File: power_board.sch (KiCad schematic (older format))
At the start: 13 parts, among them J1 CONN_01X05, P1 BATT, Q1 DMP1045U, U1 MCP73831T-2ACI_OT

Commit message: Update for LIPO power_board
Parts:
- removed Q1: DMP1045U, TO_SOT_Packages_SMD:SOT-23, symbol Device:Q_PMOS_DGS
- added H1: MH2.1mm, my-fp-library:MH2.1mm, symbol marks:MH2.1mm
- added Q1: Q_PMOS_GSD (DMP1045U), TO_SOT_Packages_SMD:SOT-23, symbol Device:Q_PMOS_GSD
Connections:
- net labels added: D, G, S, VDD
- net labels removed: VSS
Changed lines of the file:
@@
 	6500 3650 6500 3800
 Connection ~ 6150 3400
-$Comp
-L Device:Q_PMOS_DGS Q1
-U 1 1 5C2824E1
-P 7100 3500
-AR Path="/5C2824E1" Ref="Q1"  Part="1"
-AR Path="/5C2799D2/5C2824E1" Ref="Q1"  Part="1"
-F 0 "Q1" H 7300 3550 50  0000 L CNN
-F 1 "DMP1045U" H 7300 3450 50  0000 L CNN
-F 2 "TO_SOT_Packages_SMD:SOT-23" H 7300 3600 50  0001 C CNN
-F 3 "" H 7100 3500 50  0000 C CNN
-	1    7100 3500
-	0    -1   -1   0
-$EndComp
 Wire Wire Line
 	3750 3400 3750 4050
@@
 F 6 "Microchip MCP73831T-2ACI/OT" H 5150 2600 50  0001 C CNN "BOM"
 	1    5150 3200
-	1    0    0    -1
+	1    0    0    1
 $EndComp
 Connection ~ 5850 3350
@@
 	4150 3000 4150 3250
 Text GLabel 3150 3400 0    50   Input ~ 0
-VSS
+VDD
 Text GLabel 2250 3650 2    50   Input ~ 0
-VSS
+VDD
 Text GLabel 8000 3050 2    50   Output ~ 0
 +5V
@@
 Wire Wire Line
 	2400 4050 2400 4200
+$Comp
+L marks:MH2.1mm H1
+U 1 1 5C3B8630
+P 8300 4500
+F 0 "H1" H 8400 4500 60  0001 C CNN
+F 1 "MH2.1mm" H 8300 4800 60  0001 C CNN
+F 2 "my-fp-library:MH2.1mm" H 8300 4500 60  0001 C CNN
+F 3 "" H 8300 4500 60  0001 C CNN
+	1    8300 4500
+	1    0    0    -1
+$EndComp
+$Comp
+L Device:Q_PMOS_GSD Q1
+U 1 1 5C4DD92F
+P 7100 3500
+F 0 "Q1" V 7443 3500 50  0000 C CNN
+F 1 "Q_PMOS_GSD (DMP1045U)" V 7352 3500 50  0000 C CNN
+F 2 "TO_SOT_Packages_SMD:SOT-23" H 7300 3600 50  0001 C CNN
+F 3 "~" H 7100 3500 50  0001 C CNN
+	1    7100 3500
+	0    -1   -1   0
+$EndComp
+Text Label 6800 3400 0    50   ~ 0
+D
+Text Label 7100 3800 0    50   ~ 0
+G
+Text Label 7350 3400 0    50   ~ 0
+S
 $EndSCHEMATC

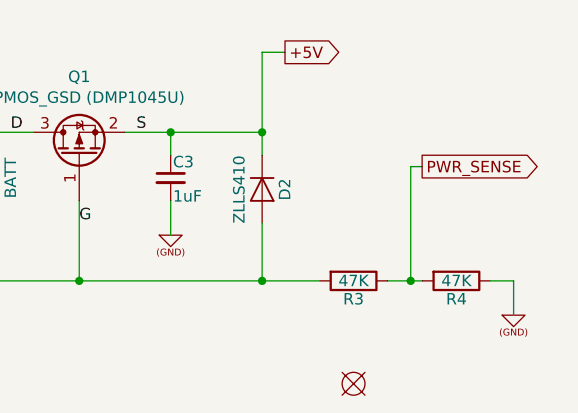
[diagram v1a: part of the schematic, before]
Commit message: Update for voltage divider to get battery level
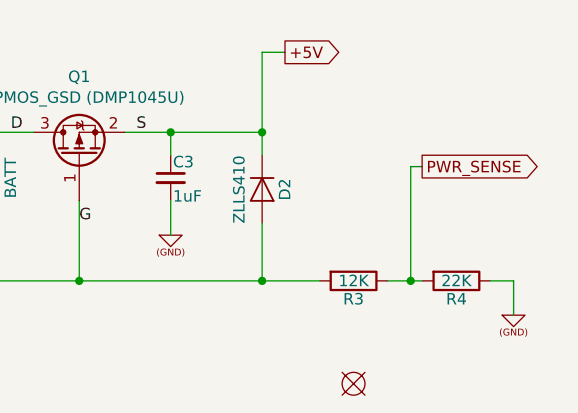
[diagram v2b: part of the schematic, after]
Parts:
- R3: value 47K -> 12K
- R4: value 47K -> 22K
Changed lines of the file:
@@
 AR Path="/5C2799D2/5C282508" Ref="R9"  Part="1"
 F 0 "R3" V 8380 4050 50  0000 C CNN
-F 1 "47K" V 8300 4050 50  0000 C CNN
+F 1 "12K" V 8300 4050 50  0000 C CNN
 F 2 "Resistors_SMD:R_0805_HandSoldering" V 8230 4050 50  0001 C CNN
 F 3 "" H 8300 4050 50  0000 C CNN
@@
 AR Path="/5C2799D2/5C282515" Ref="R10"  Part="1"
 F 0 "R4" V 8830 4050 50  0000 C CNN
-F 1 "47K" V 8750 4050 50  0000 C CNN
+F 1 "22K" V 8750 4050 50  0000 C CNN
 F 2 "Resistors_SMD:R_0805_HandSoldering" V 8680 4050 50  0001 C CNN
 F 3 "" H 8750 4050 50  0000 C CNN
